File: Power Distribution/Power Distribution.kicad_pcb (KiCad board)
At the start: 16 copper layers, 61 x 88 mm, 28 parts, among them IC3 PCM5102 Audio Stereo DAC

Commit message: updated schematic and PCB
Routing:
- net (no net): track 1198.5 -> 1051.0 mm

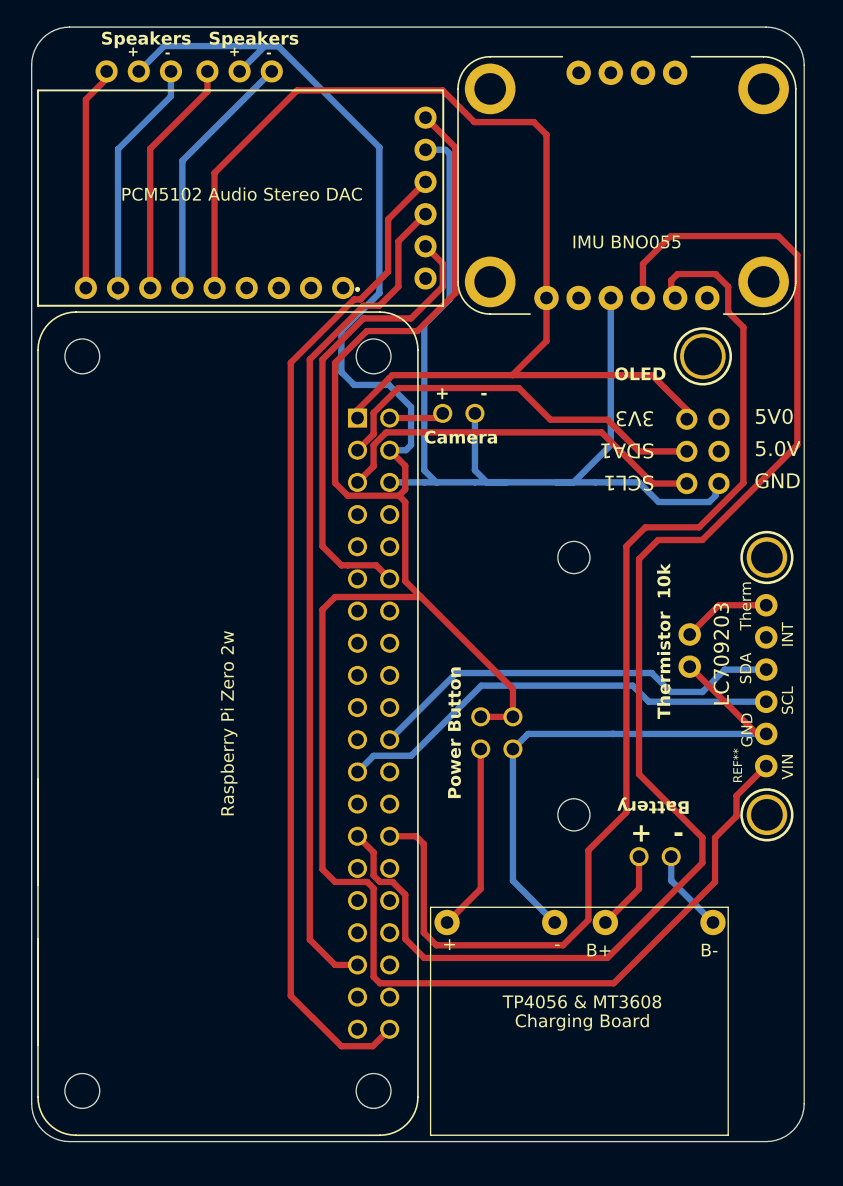
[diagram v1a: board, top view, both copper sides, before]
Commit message: Updated schematic and PCB
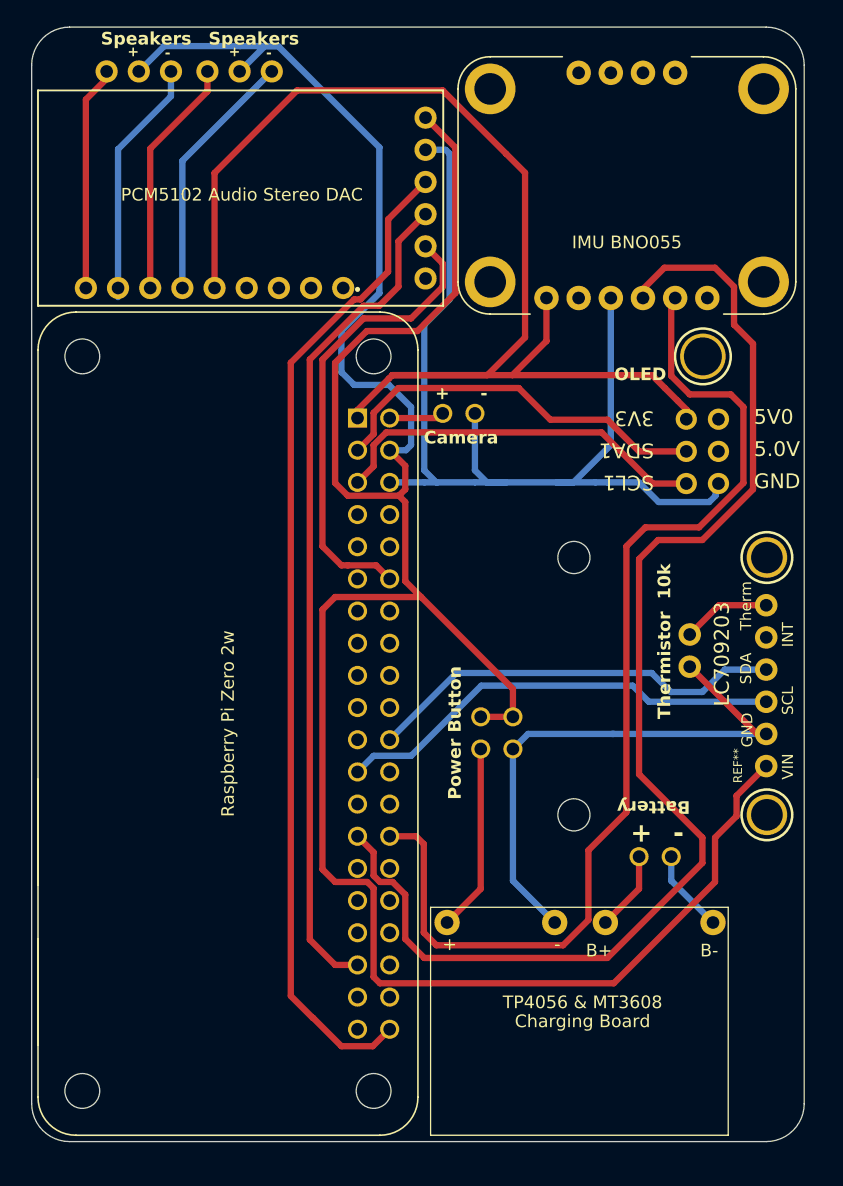
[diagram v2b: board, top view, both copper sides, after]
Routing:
- net (no net): track 1051.0 -> 1048.8 mm

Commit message: PCB
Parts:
- removed the REF** at (260.5, 100.0)
- removed UNK_HOLE_0: , LC709203F:dummyfp0
- removed UNK_HOLE_1: , LC709203F:dummyfp1
- added ?: , , F.Cu at (248.2, 99.5)
- added ?: , , F.Cu at (224.5, 118.8)
- added ?: , , F.Cu at (256.0, 118.2)
- added ?: , , F.Cu at (245.0, 134.5)
- added ?: , , F.Cu at (222.5, 126.8)
- added ?: , , F.Cu at (241.5, 134.5)
- added ?: , , F.Cu at (218.8, 146.2)
- added ?: , , F.Cu at (246.5, 91.5)
- added ?: , , F.Cu at (218.8, 153.0)
- added ?: , , F.Cu at (246.5, 115.2)
- added ?: , , F.Cu at (218.2, 129.0)
- added ?: , , F.Cu at (248.2, 115.2)
- added ?: , , F.Cu at (244.8, 112.2)
- added ?: , , F.Cu at (244.8, 109.3)
- added ?: , , F.Cu at (224.5, 122.5)
- added ?: , , F.Cu at (262.0, 118.2)
- added ?: , , F.Cu at (256.8, 124.8)
- added ?: , , F.Cu at (256.8, 126.8)
- moved ? 15.0 mm to (242.8, 119.5)
- moved ? 15.0 mm to (240.3, 119.5)
- moved ? 11.3 mm to (253.5, 115.0), turned to -90 degrees
- moved ? 7.79 mm to (256.0, 115.0), turned to -90 degrees
- moved G*** 0.84 mm to (219.8, 157.4)
- turned REF** to 90 degrees
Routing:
- net (no net): track 1048.8 -> 905.4 mm
- added copper zone on B.Cu, net (none)
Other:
- board text added: "USB ↓"

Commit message: PCB
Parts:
- removed U$19, U$21: MOUNTINGHOLE2.5, LC709203F:MOUNTINGHOLE_2.5_PLATED
- added ?: , , F.Cu at (252.6, 121.7)
- added ?: , , F.Cu at (250.1, 121.7)
- REF**: value Raspberry Pi Zero 2w -> MODULE_SC1176
- REF**: value IMU BNO055 -> MODULE_2472
- moved ? 3.60 mm to (248.6, 134.6)
- moved ? 0.67 mm to (244.2, 109.7)
- moved ? 0.55 mm to (244.2, 112.3)
- moved ? 0.50 mm to (246.0, 91.5)
- moved ? 0.40 mm to (246.1, 115.2)
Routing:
- net (no net): track 905.4 -> 895.9 mm
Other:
- board text added: "Capacitor 10nF"
- board text added: "IMU BNO055"
- board text added: "Pin1"
- board text added: "Pin40"
- board text added: "Raspberry Pi Zero 2w"

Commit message: PCB
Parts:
- removed the ? at (224.5, 118.8)
- removed the ? at (248.6, 134.6)
- removed the ? at (218.8, 146.2)
- removed the ? at (218.8, 153.0)
- removed the ? at (241.5, 134.5)
- removed the ? at (224.5, 122.5)
- added ?: , , F.Cu at (225.7, 138.5)
- added ?: , , F.Cu at (219.8, 100.9)
- added ?: , , F.Cu at (225.7, 136.9)
- added ?: , , F.Cu at (244.2, 107.8)
- added ?: , , F.Cu at (228.4, 109.9)
- added ?: , , F.Cu at (230.5, 112.5)
- added ?: , , F.Cu at (232.1, 138.4)
- added ?: , , F.Cu at (226.1, 102.9)
- added ?: , , F.Cu at (216.0, 105.6)
- added ?: , , F.Cu at (230.3, 136.9)
- added ?: , , F.Cu at (234.6, 120.3)
- added ?: , , F.Cu at (228.4, 118.0)
- added ?: , , F.Cu at (216.0, 157.3)
- added ?: , , F.Cu at (244.2, 112.4)
- REF**: moved to B.Cu
- moved G*** 42.2 mm to (262.0, 157.1)
- moved ? 16.5 mm to (228.4, 107.4)
- moved ? 7.42 mm to (218.2, 132.8)
- moved ? 1.10 mm to (219.0, 128.2)
- turned REF** to -90 degrees
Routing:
- net (no net): track 895.9 -> 926.9 mm

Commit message: PCB
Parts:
- removed the ? at (248.2, 99.5)
- removed the ? at (225.7, 138.5)
- removed the ? at (219.8, 100.9)
- removed the ? at (225.7, 136.9)
- removed the ? at (256.0, 118.2)
- removed the ? at (244.2, 107.8)
- removed the ? at (228.4, 109.9)
- removed the ? at (230.5, 112.5)
- removed the ? at (232.1, 138.4)
- removed the ? at (218.2, 132.8)
- removed the ? at (226.1, 102.9)
- removed the ? at (216.0, 105.6)
- removed the ? at (230.3, 136.9)
- removed the ? at (248.2, 115.2)
- removed the ? at (234.6, 120.3)
- removed the ? at (246.0, 91.5)
- removed the ? at (246.1, 115.2)
- removed the ? at (228.4, 118.0)
- removed the ? at (219.0, 128.2)
- removed the ? at (216.0, 157.3)
- removed the ? at (228.4, 107.4)
- removed the ? at (244.2, 109.7)
- removed the ? at (244.2, 112.4)
- removed the ? at (262.0, 118.2)
- removed the ? at (256.8, 124.8)
- removed the ? at (256.8, 126.8)
- added ?: , , F.Cu at (241.5, 132.5)
- added ?: , , F.Cu at (243.2, 100.6)
- added ?: , , F.Cu at (243.2, 103.4)
- added ?: , , F.Cu at (233.5, 132.5)
- added ?: , , F.Cu at (244.5, 129.0)
- added ?: , , F.Cu at (246.0, 122.0)
- added ?: , , F.Cu at (251.0, 129.5)
- added ?: , , F.Cu at (245.8, 111.2)
- added ?: , , F.Cu at (238.5, 139.0)
- added ?: , , F.Cu at (245.8, 114.0)
- added ?: , , F.Cu at (240.3, 111.2)
- added ?: , , F.Cu at (241.6, 119.2)
- added ?: , , F.Cu at (240.5, 122.0)
- added ?: , , F.Cu at (246.0, 119.2)
- added ?: , , F.Cu at (237.7, 100.6)
- added ?: , , F.Cu at (236.5, 129.0)
- added ?: , , F.Cu at (237.7, 103.4)
- added ?: , , F.Cu at (240.3, 114.0)
- moved ? 79.9 mm to (247.6, 149.7), turned to 180 degrees
- moved ? 76.5 mm to (247.6, 147.1), turned to 180 degrees
- moved ? 73.1 mm to (247.6, 144.6), turned to 180 degrees
- moved ? 69.4 mm to (247.6, 141.7), turned to 180 degrees
- moved ? 66.1 mm to (247.6, 139.2), turned to 180 degrees
- moved ? 62.8 mm to (247.6, 136.6), turned to 180 degrees
- moved ? 49.4 mm to (212.0, 158.0), turned to 0 degrees
- moved IC3 48.9 mm to (264.7, 131.0), turned to -90 degrees
- moved ? 45.8 mm to (212.0, 155.5), turned to 0 degrees
- moved ? 44.2 mm to (212.0, 144.2)
- moved ? 44.2 mm to (214.6, 144.2)
- moved REF** 39.0 mm to (261.5, 87.2)
- moved ? 36.1 mm to (214.5, 149.5)
- moved ? 36.1 mm to (212.0, 149.5)
- moved ? 36.1 mm to (214.5, 147.0)
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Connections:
- ? pad 2: (no net) -> GND (x3)
- ? pad 3: (no net) -> GND (x3)
- ? pad 2: (no net) -> 5V (x3)
- ? pad 4: (no net) -> 5V
- ? pad 1: (no net) -> 5V
- ? pad 1: (no net) -> GND
- IC3 pad 1: (no net) -> 5V
- IC3 pad 12: (no net) -> GND
- IC3 pad 14: (no net) -> GND
- IC3 pad 2: (no net) -> GND
- IC3 pad 4: (no net) -> Signals
- IC3 pad 5: (no net) -> Signals
- REF** pad 1: (no net) -> 5V (x2)
- REF** pad 2: (no net) -> GND
- REF** pad 4: (no net) -> 5V (x2)
- REF** pad 6: (no net) -> GND (x2)
- REF** pad 3: (no net) -> GND
- REF** pad 12: (no net) -> Signals
- REF** pad 14: (no net) -> GND
- REF** pad 2: (no net) -> 5V
- REF** pad 20: (no net) -> GND
- REF** pad 22: (no net) -> Signals
- REF** pad 23: (no net) -> Signals
- REF** pad 25: (no net) -> GND
- REF** pad 27: (no net) -> Signals
- REF** pad 28: (no net) -> Signals
- REF** pad 3: (no net) -> Signals
- REF** pad 30: (no net) -> GND
- REF** pad 34: (no net) -> GND
- REF** pad 39: (no net) -> GND
- REF** pad 5: (no net) -> Signals
- REF** pad 9: (no net) -> GND
- TP4056 & MT3608 pad 2: (no net) -> GND
- TP4056 & MT3608 pad 4: (no net) -> GND
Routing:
- net (no net): track 926.9 -> 149.2 mm
- net Signals: track 0.00 -> 370.7 mm
- net 5V: track 0.00 -> 316.0 mm
- added copper zone on B.Cu, net GND
- removed copper zone on B.Cu, net (none)

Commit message: PCB
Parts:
- moved TP4056 & MT3608 1.08 mm to (228.0, 147.7)
- moved ? 1.08 mm to (233.2, 140.7)
- moved ? 1.08 mm to (235.8, 140.7)
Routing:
- net (no net): track 149.2 -> 146.5 mm
- net 5V: track 316.0 -> 315.5 mm
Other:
- board text removed: "Battery"
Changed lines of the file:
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@@
 	(footprint "ChargingBoardTP4056:Charging Board TP4056"
 		(layer "F.Cu")
-		(at 228.7 148.525)
+		(at 227.97 147.73)
 		(property "Reference" "TP4056 & MT3608"
 			(at 1 2 0)
@@
 	(footprint ""
 		(layer "F.Cu")
-		(at 236.5 141.5 90)
+		(at 235.77 140.705 90)
 		(property "Reference" ""
 			(at 0 0 90)
@@
 	(footprint ""
 		(layer "F.Cu")
-		(at 233.96 141.5 90)
+		(at 233.23 140.705 90)
 		(property "Reference" ""
 			(at 0 0 90)
@@
 		(layer "Edge.Cuts")
 	)
-	(gr_text "Pin40"
-		(at 208.8 132.6 0)
+	(gr_text "+"
+		(at 211.4 142.5 270)
 		(layer "F.SilkS")
 		(effects
@@
 				(bold yes)
 			)
-			(justify left bottom)
+			(justify left bottom mirror)
 		)
 	)
-	(gr_text "Battery"
-		(at 238 137 180)
+	(gr_text "Pin40"
+		(at 208.8 132.6 0)
 		(layer "F.SilkS")
 		(effects
@@
 	)
 	(gr_text "Capacitor 10nF"
-		(at 214.04 142.16 0)
+		(at 214.04 140 0)
 		(layer "F.SilkS")
 		(effects
@@
 		)
 	)
+	(gr_text "-"
+		(at 267.8 84 270)
+		(layer "F.SilkS")
+		(effects
+			(font
+				(size 0.8 0.8)
+				(thickness 0.16)
+				(bold yes)
+			)
+			(justify left bottom mirror)
+		)
+	)
 	(gr_text "SCL"
 		(at 263.207 88.373 90)
@@
 		)
 	)
+	(gr_text "-"
+		(at 215.35 142.3 0)
+		(layer "F.SilkS")
+		(effects
+			(font
+				(size 1 1)
+				(thickness 0.25)
+				(bold yes)
+			)
+			(justify left bottom mirror)
+		)
+	)
 	(gr_text "Camera"
 		(at 209.5 153.96 270)
@@
 		)
 	)
+	(gr_text "+"
+		(at 267.8 81.4 270)
+		(layer "F.SilkS")
+		(effects
+			(font
+				(size 0.8 0.8)
+				(thickness 0.16)
+				(bold yes)
+			)
+			(justify left bottom mirror)
+		)
+	)
 	(gr_text "LC709203"
 		(at 258 84.69 90)
@@
 	)
 	(gr_text "-\n"
-		(at 237.5 140.5 0)
+		(at 236.8 139.4 0)
 		(layer "F.SilkS")
 		(effects
@@
 		)
 	)
+	(gr_text "GND"
+		(at 217.3 151.2 90)
+		(layer "F.SilkS")
+		(effects
+			(font
+				(size 1 1)
+				(thickness 0.25)
+				(bold yes)
+			)
+			(justify left bottom)
+		)
+	)
 	(gr_text "Speakers\n"
 		(at 245.64 141.64 90)
@@
 	)
 	(gr_text "+\n"
-		(at 235 140.5 0)
+		(at 234.2 139.2 0)
 		(layer "F.SilkS")
 		(effects
@@
 	)
 	(segment
-		(start 254 131)
-		(end 214 131)
+		(start 214.77 81.37)
+		(end 230.37 81.37)
+		(width 0.8)
+		(layer "F.Cu")
+		(net 0)
+	)
+	(segment
+		(start 218.27 143.43)
+		(end 218.27 150.63)
 		(width 0.7)
 		(layer "F.Cu")
@@
 	)
 	(segment
-		(start 214.77 81.37)
-		(end 230.37 81.37)
-		(width 0.8)
+		(start 254 131)
+		(end 256.37 128.63)
+		(width 0.7)
 		(layer "F.Cu")
 		(net 0)
 	)
 	(segment
-		(start 214.96 152.5)
-		(end 217.5 152.5)
-		(width 0.8)
+		(start 212.23 129.63)
+		(end 213.6 131)
+		(width 0.7)
 		(layer "F.Cu")
 		(net 0)
@@
 	)
 	(segment
-		(start 231.5 144.225)
-		(end 233.96 141.765)
+		(start 230.77 143.43)
+		(end 233.23 140.97)
 		(width 0.8)
 		(layer "F.Cu")
@@
 	)
 	(segment
-		(start 256.37 124.54)
-		(end 256.37 128.63)
-		(width 0.7)
+		(start 247.64 141.72)
+		(end 249.22 141.72)
+		(width 0.6)
 		(layer "F.Cu")
 		(net 0)
 	)
 	(segment
-		(start 256.37 128.63)
+		(start 213.6 131)
 		(end 254 131)
 		(width 0.7)
@@
 	)
 	(segment
-		(start 247.64 141.72)
-		(end 249.22 141.72)
-		(width 0.6)
-		(layer "F.Cu")
-		(net 0)
-	)
-	(segment
-		(start 219 151)
-		(end 219 144.225)
-		(width 0.8)
+		(start 256.37 128.63)
+		(end 256.37 124.54)
+		(width 0.7)
 		(layer "F.Cu")
 		(net 0)
@@
 	)
 	(segment
-		(start 216.5 152.5)
-		(end 217.5 152.5)
-		(width 0.8)
-		(layer "F.Cu")
-		(net 0)
-	)
-	(segment
-		(start 253.78 146.28)
-		(end 264.74 146.28)
-		(width 0.6)
+		(start 218.27 150.63)
+		(end 216.4 152.5)
+		(width 0.7)
 		(layer "F.Cu")
 		(net 0)
 	)
 	(segment
-		(start 214 131)
-		(end 213.6 131)
+		(start 215 152.5)
+		(end 216.4 152.5)
 		(width 0.7)
 		(layer "F.Cu")
@@
 	)
 	(segment
-		(start 233.96 141.765)
-		(end 233.96 141.5)
-		(width 0.8)
+		(start 253.78 146.28)
+		(end 264.74 146.28)
+		(width 0.6)
 		(layer "F.Cu")
 		(net 0)
 	)
 	(segment
-		(start 217.5 152.5)
-		(end 219 151)
+		(start 233.23 140.97)
+		(end 233.23 140.705)
 		(width 0.8)
 		(layer "F.Cu")
@@
 	)
 	(segment
-		(start 213.6 131)
-		(end 212.23 129.63)
-		(width 0.7)
-		(layer "F.Cu")
-		(net 0)
-	)
-	(segment
-		(start 215 152.5)
-		(end 216.5 152.5)
-		(width 0.8)
-		(layer "F.Cu")
-		(net 0)
-	)
-	(segment
 		(start 249.9 151.36)
 		(end 264.74 151.36)
@@
 	(segment
 		(start 228.5 137.5)
-		(end 234 137.5)
-		(width 0.8)
-		(layer "F.Cu")
-		(net 2)
-	)
-	(segment
-		(start 236.5 137.5)
-		(end 241.5 132.5)
-		(width 0.8)
-		(layer "F.Cu")
-		(net 2)
-	)
-	(segment
-		(start 241.5 137.5)
-		(end 245.96 137.5)
-		(width 0.8)
+		(end 236.5 137.5)
+		(width 0.7)
 		(layer "F.Cu")
 		(net 2)
@@
 	)
 	(segment
-		(start 223.5 137.5)
-		(end 224 137.5)
-		(width 0.8)
-		(layer "F.Cu")
-		(net 2)
-	)
-	(segment
 		(start 212.04 144.16)
 		(end 212.04 146.92)
@@
 	(segment
 		(start 217 137.5)
-		(end 218.5 137.5)
+		(end 228.5 137.5)
 		(width 0.8)
 		(layer "F.Cu")
@@
 	)
 	(segment
+		(start 245.96 137.5)
+		(end 247.64 139.18)
+		(width 0.7)
+		(layer "F.Cu")
+		(net 2)
+	)
+	(segment
 		(start 243 106.5)
 		(end 255.96 93.54)
@@
 	)
 	(segment
-		(start 236.5 137.5)
+		(start 245 141)
 		(end 241.5 137.5)
-		(width 0.8)
+		(width 0.7)
 		(layer "F.Cu")
 		(net 2)
@@
 	)
 	(segment
-		(start 217.2 139)
-		(end 238.5 139)
-		(width 0.8)
+		(start 241.5 137.5)
+		(end 245.96 137.5)
+		(width 0.7)
 		(layer "F.Cu")
 		(net 2)
 	)
 	(segment
-		(start 243 122.5)
-		(end 243 106.5)
-		(width 0.8)
+		(start 236.5 137.5)
+		(end 241.5 132.5)
+		(width 0.7)
 		(layer "F.Cu")
 		(net 2)
 	)
 	(segment
-		(start 234 137.5)
+		(start 241.5 137.5)
 		(end 236.5 137.5)
-		(width 0.8)
+		(width 0.7)
 		(layer "F.Cu")
 		(net 2)
 	)
 	(segment
-		(start 209 87.14)
-		(end 212.23 83.91)
+		(start 217.2 139)
+		(end 238.5 139)
 		(width 0.8)
 		(layer "F.Cu")
@@
 	)
 	(segment
-		(start 251 129.5)
-		(end 251 124.83)
+		(start 243 122.5)
+		(end 243 106.5)
 		(width 0.8)
 		(layer "F.Cu")
@@
 	)
 	(segment
-		(start 218.5 137.5)
-		(end 223.5 137.5)
+		(start 209 87.14)
+		(end 212.23 83.91)
 		(width 0.8)
 		(layer "F.Cu")
@@
 	)
 	(segment
-		(start 212.04 144.16)
-		(end 209 141.12)
+		(start 251 129.5)
+		(end 251 124.83)
 		(width 0.8)
 		(layer "F.Cu")
@@
 	)
 	(segment
-		(start 248.61 103.65)
-		(end 244.5 107.76)
+		(start 212.04 144.16)
+		(end 209 141.12)
 		(width 0.8)
 		(layer "F.Cu")
@@
 	)
 	(segment
-		(start 223.5 137.5)
-		(end 228.5 137.5)
+		(start 248.61 103.65)
+		(end 244.5 107.76)
 		(width 0.8)
 		(layer "F.Cu")
@@
 	)
 	(segment
-		(start 245.96 137.5)
-		(end 247.64 139.18)
-		(width 0.8)
-		(layer "F.Cu")
-		(net 2)
-	)
-	(segment
 		(start 233.5 132.5)
 		(end 228.5 137.5)
 		(width 0.8)
 		(layer "F.Cu")
-		(net 2)
-	)
-	(segment
-		(start 241.5 137.5)
-		(end 245 141)
-		(width 0.8)
-		(layer "F.Cu")

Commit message: PCB
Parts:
- moved REF** 11.8 mm to (241.7, 83.8)
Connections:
- REF** pad 3: (no net) -> Signals
- REF** pad 5: (no net) -> Signals
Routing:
- net Signals: track 370.7 -> 358.2 mm
- net (no net): track 146.5 -> 140.3 mm
- net 5V: track 315.5 -> 311.8 mm
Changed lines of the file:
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@@
 	(footprint "Adafruit 128x32 Pi OLED:RASPBERRYPI_2X3_THMSMT"
 		(layer "F.Cu")
-		(at 243.23 95.5)
+		(at 241.73 83.76)
 		(property "Reference" "REF**"
 			(at 0 0 0)
@@
 			(layers "*.Cu" "*.Mask")
 			(remove_unused_layers no)
+			(net 3 "Signals")
 			(solder_mask_margin 0.0508)
 			(thermal_bridge_angle 0)
@@
 			(layers "*.Cu" "*.Mask")
 			(remove_unused_layers no)
+			(net 3 "Signals")
 			(solder_mask_margin 0.0508)
 			(thermal_bridge_angle 0)
@@
 	)
 	(gr_text "OLED"
-		(at 237.96 91.5 0)
+		(at 236.46 79.76 0)
 		(layer "F.SilkS")
 		(effects
@@
 	)
 	(segment
-		(start 214.77 81.37)
-		(end 230.37 81.37)
-		(width 0.8)
-		(layer "F.Cu")
-		(net 0)
-	)
-	(segment
 		(start 218.27 143.43)
 		(end 218.27 150.63)
@@
 		(start 254 131)
 		(end 256.37 128.63)
+		(width 0.7)
+		(layer "F.Cu")
+		(net 0)
+	)
+	(segment
+		(start 214.77 81.37)
+		(end 240.31 81.37)
 		(width 0.7)
 		(layer "F.Cu")
@@
 	)
 	(segment
-		(start 230.37 81.37)
-		(end 241.96 92.96)
-		(width 0.8)
-		(layer "F.Cu")
-		(net 0)
-	)
-	(segment
 		(start 218.27 150.63)
 		(end 216.4 152.5)
@@
 	)
 	(segment
+		(start 240.31 81.37)
+		(end 240.46 81.22)
+		(width 0.7)
+		(layer "F.Cu")
+		(net 0)
+	)
+	(segment
 		(start 249.9 151.36)
 		(end 264.74 151.36)
@@
 	)
 	(segment
-		(start 246.5 93.5)
-		(end 244.5 95.5)
-		(width 0.8)
-		(layer "F.Cu")
-		(net 2)
-	)
-	(segment
 		(start 245 144.5)
 		(end 247.64 147.14)
@@
 	)
 	(segment
-		(start 246.5 91)
-		(end 235 79.5)
-		(width 0.8)
-		(layer "F.Cu")
-		(net 2)
-	)
-	(segment
 		(start 228.5 137.5)
 		(end 236.5 137.5)
@@
 	)
 	(segment
+		(start 244.84 83.76)
+		(end 243 83.76)
+		(width 0.7)
+		(layer "F.Cu")
+		(net 2)
+	)
+	(segment
 		(start 209 141.12)
 		(end 209 87.14)
@@
 	)
 	(segment
-		(start 214.1 79.5)
-		(end 235 79.5)
-		(width 0.8)
-		(layer "F.Cu")
-		(net 2)
-	)
-	(segment
 		(start 212.04 144.16)
 		(end 212.04 146.92)
@@
 	)
 	(segment
-		(start 246.5 93.5)
-		(end 246.5 91)
-		(width 0.8)
-		(layer "F.Cu")
-		(net 2)
-	)
-	(segment
 		(start 251 124.83)
 		(end 251.29 124.54)
@@
 	)
 	(segment
+		(start 246.4 82.2)
+		(end 244.84 83.76)
+		(width 0.7)
+		(layer "F.Cu")
+		(net 2)
+	)
+	(segment
+		(start 245.25 79.2)
+		(end 246.4 80.35)
+		(width 0.7)
+		(layer "F.Cu")
+		(net 2)
+	)
+	(segment
 		(start 243 106.5)
 		(end 255.96 93.54)
@@
 	)
 	(segment
+		(start 214.4 79.2)
+		(end 245.25 79.2)
+		(width 0.7)
+		(layer "F.Cu")
+		(net 2)
+	)
+	(segment
 		(start 212.04 144.16)
 		(end 209 141.12)
@@
 	)
 	(segment
+		(start 246.4 80.35)
+		(end 246.4 82.2)
+		(width 0.7)
+		(layer "F.Cu")
+		(net 2)
+	)
+	(segment
 		(start 244.5 107.76)
 		(end 244.5 129)
@@
 	)
 	(segment
-		(start 212.23 81.37)
-		(end 214.1 79.5)
-		(width 0.8)
-		(layer "F.Cu")
-		(net 2)
-	)
-	(segment
 		(start 233.5 132.5)
 		(end 228.5 137.5)
@@
 	)
 	(segment
+		(start 212.23 81.37)
+		(end 214.4 79.2)
+		(width 0.7)
+		(layer "F.Cu")
+		(net 2)
+	)
+	(segment
 		(start 233.5 132.5)
 		(end 233.5 132)
@@
 	)
 	(segment
+		(start 214.77 83.91)
+		(end 240.31 83.91)
+		(width 0.7)
+		(layer "F.Cu")
+		(net 3)
+	)
+	(segment
+		(start 214.77 86.45)
+		(end 240.31 86.45)
+		(width 0.7)
+		(layer "F.Cu")
+		(net 3)
+	)
+	(segment
 		(start 243.2 103.4)
 		(end 243.8 103.4)
@@
 	)
 	(segment
-		(start 214.77 83.91)
-		(end 230.37 83.91)
-		(width 0.7)
-		(layer "F.Cu")
-		(net 3)
-	)
-	(segment
 		(start 215.8 105.6)
 		(end 213.4 105.6)
@@
 	)
 	(segment
-		(start 230.37 83.91)
-		(end 241.96 95.5)
-		(width 0.7)
-		(layer "F.Cu")
-		(net 3)
-	)
-	(segment
 		(start 258.91 124.54)
 		(end 258.91 122.91)
@@
 	)
 	(segment
+		(start 240.31 86.45)
+		(end 240.46 86.3)
+		(width 0.7)
+		(layer "F.Cu")
+		(net 3)
+	)
+	(segment
 		(start 243.2 100.6)
 		(end 244.8 100.6)
@@
 	)
 	(segment
+		(start 240.31 83.91)
+		(end 240.46 83.76)
+		(width 0.7)
+		(layer "F.Cu")
+		(net 3)
+	)
+	(segment
 		(start 248.42 114)
 		(end 248.61 113.81)
@@
 	)
 	(segment
-		(start 230.37 86.45)
-		(end 241.96 98.04)
-		(width 0.7)
-		(layer "F.Cu")
-		(net 3)
-	)
-	(segment
 		(start 243.8 103.4)
 		(end 258.74 88.46)
@@
 		(width 0.7)
 		(layer "F.Cu")
-		(net 3)
-	)
-	(segment
-		(start 214.77 86.45)
-		(end 230.37 86.45)
-		(width 0.7)
-		(layer "F.Cu")
